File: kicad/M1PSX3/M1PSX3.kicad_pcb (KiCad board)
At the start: 2 copper layers, 60 x 81 mm, 10 parts, among them J1 Conn_01x02, J2 1x5, J3 DIN5, J4 Conn_01x02, T1 DST-6-16

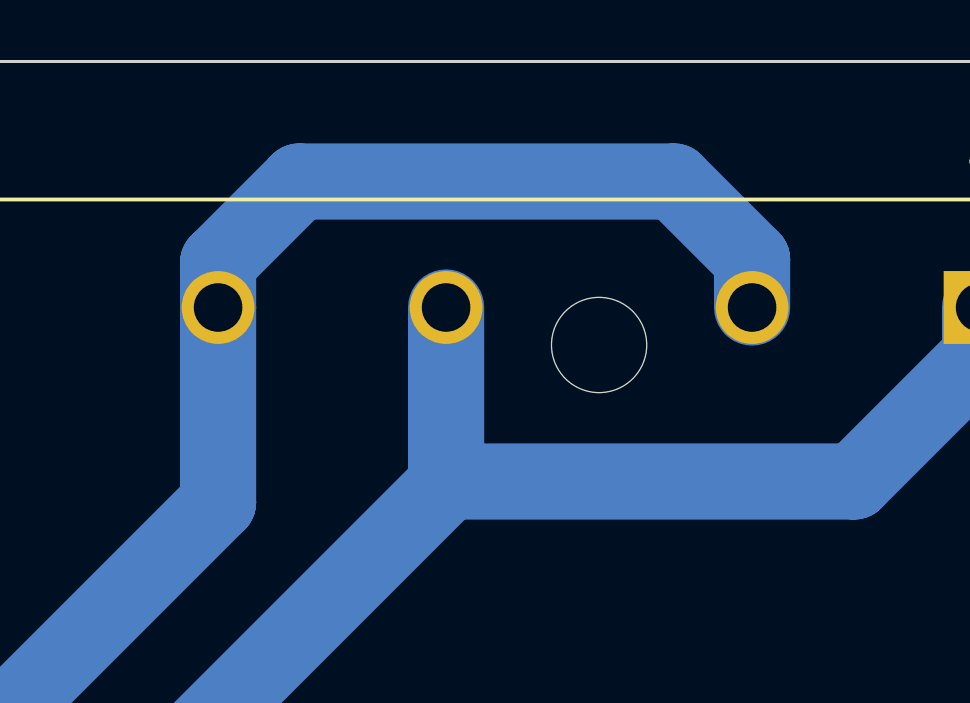
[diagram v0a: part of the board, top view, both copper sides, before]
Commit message: Tweaked design for 110V single primary transformer option or 220V dual primary transformer option.
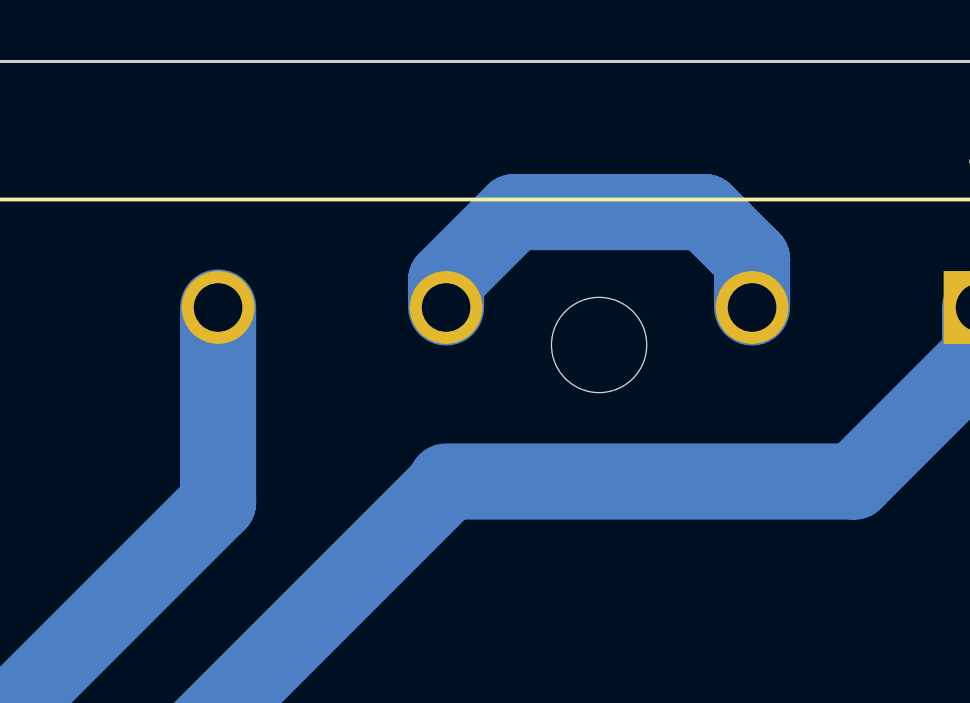
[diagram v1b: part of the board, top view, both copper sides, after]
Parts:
- R1: value 1.5k -> 2.4k
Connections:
- T1 pad 2: Net-(J1-Pin_1) -> Net-(T1-Pad2)
- T1 pad 3: Net-(J1-Pin_2) -> Net-(T1-Pad2)
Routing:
- net Net-(J1-Pin_1): track 86.3 -> 63.3 mm
- net Net-(T1-Pad2): track 0.00 -> 14.3 mm
- net Net-(J1-Pin_2): track 85.0 -> 79.1 mm
